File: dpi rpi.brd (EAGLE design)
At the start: 54.5 x 21.2 mm, 12 parts, among them U3 FAN5333BSX

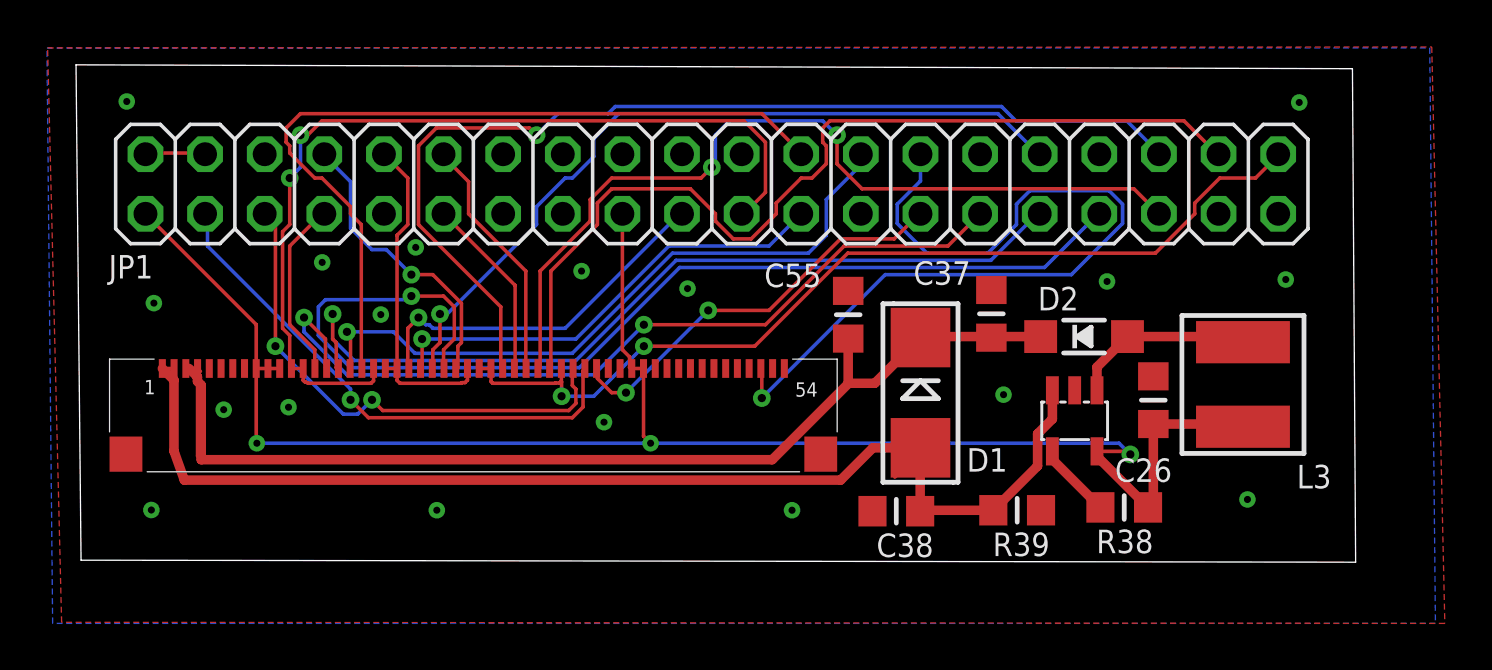
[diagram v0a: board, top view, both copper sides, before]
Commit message: Add files via upload
Updated with Helders tidy up of the crappy auto-routing for RGB lines.
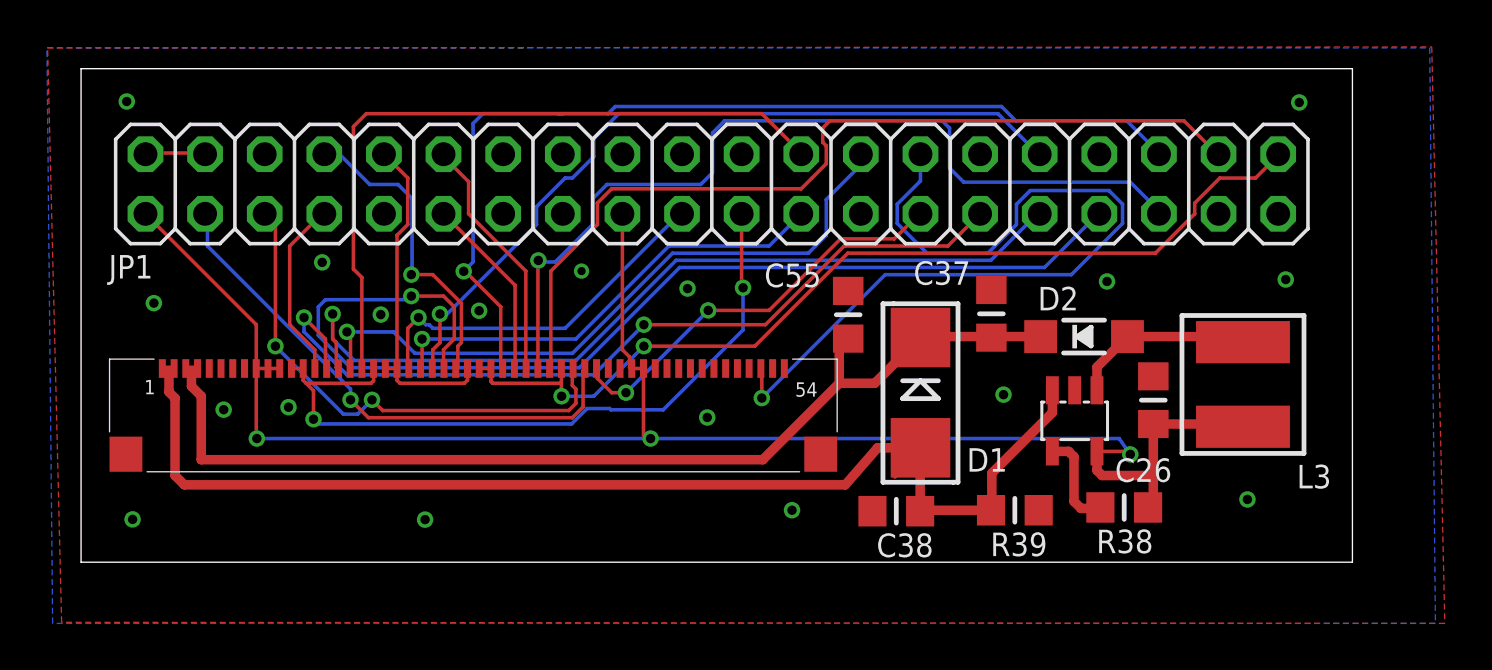
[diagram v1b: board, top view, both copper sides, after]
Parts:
- moved R39 0.10 mm to (39.6, 82.6)
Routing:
- net B5: track 39.0 -> 31.3 mm
- net B4: track 34.7 -> 30.6 mm
- net +24V: track 53.7 -> 50.1 mm
- net R0: track 44.4 -> 41.9 mm
- net R4: track 39.7 -> 37.5 mm
- net R3: track 36.8 -> 38.2 mm, vias 2 -> 1
- net PWM: track 3.24 -> 4.53 mm
- net LEDK: track 53.7 -> 54.6 mm
- net G4: track 12.6 -> 13.3 mm
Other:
- board size 54.5 x 21.2 mm -> 54.2 x 21 mm
